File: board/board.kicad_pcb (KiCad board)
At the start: 2 copper layers, 26.5 x 7.5 mm, 10 parts, among them Q1 2N7002, U1 ATtiny402-SS

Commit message: fixed schematic and pcb
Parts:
- added C3: 10u, Capacitor_SMD:C_0603_1608Metric_Pad1.08x0.95mm_HandSolder, F.Cu at (99.1, 76.0)
- added G***: LOGO, LOGO, B.Cu at (84.3, 77.8)
- added TP1: TestPoint, TestPoint:TestPoint_Pad_D1.0mm, B.Cu at (96.3, 80.3)
- Q1: value 2N7002 -> AO3401A
- moved Q1 0.63 mm to (99.1, 78.8), turned to -90 degrees
- moved U3 0.55 mm to (103.4, 82.3)
- moved R1 0.44 mm to (94.6, 77.6)
- moved R2 0.44 mm to (94.6, 76.2), turned to 180 degrees
- moved R3 0.44 mm to (94.6, 79.1)
- moved R4 0.44 mm to (94.6, 80.5)
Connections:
- C2 pad 2: GND_BT -> GND
- Q1 pad 2: GND -> +4V
- Q1 pad 3: GND_BT -> Vcc_BT
- R2 pad 1: GND -> Net-(Q1-G)
- R2 pad 2: Net-(Q1-G) -> +4V
- U1 pad 2: unconnected-(U1-PA6-Pad2) -> IO_SCAN
- U3 pad 1: +4V -> Vcc_BT
- U3 pad 3: UPDI -> IO_SCAN
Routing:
- net IO_SCAN: track 0.00 -> 17.8 mm, vias 0 -> 2
- net GND_BT: track 10.4 -> 0.00 mm
- net Vcc_BT: track 0.00 -> 10.3 mm
- net GND: track 11.9 -> 3.34 mm, vias 5 -> 3
- net UPDI: track 9.41 -> 3.62 mm, vias 0 -> 1
- net INT_SW: track 20.5 -> 15.0 mm
- net +4V: track 27.1 -> 22.9 mm, vias 2 -> 4
- net Net-(Q1-G): track 6.41 -> 8.00 mm
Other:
- board size 26.5 x 7.5 mm -> 26 x 7.5 mm

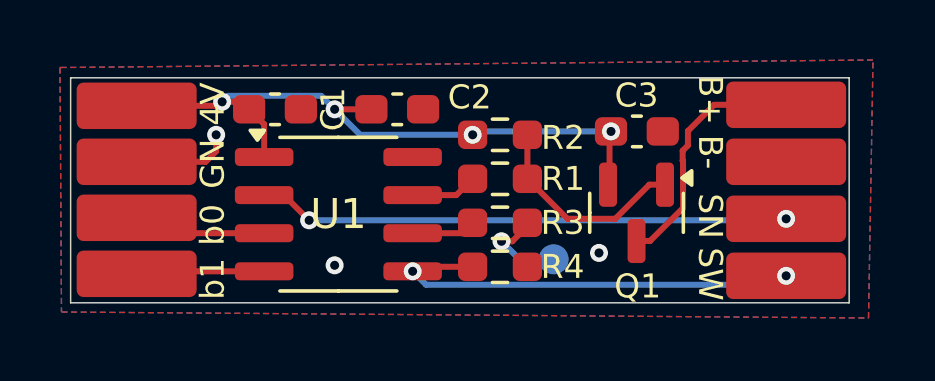
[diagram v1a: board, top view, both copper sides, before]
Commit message: pcb tweaks and gitignore
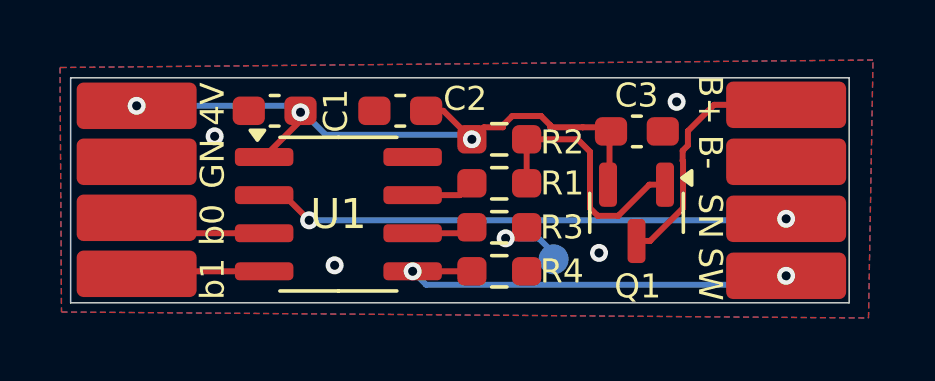
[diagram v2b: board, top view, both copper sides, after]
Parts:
- moved R3 0.15 mm to (94.5, 79.2)
- moved R4 0.15 mm to (94.5, 80.7)
- moved R1 0.15 mm to (94.5, 77.8)
- moved R2 0.15 mm to (94.5, 76.3)
- moved C2 0.11 mm to (91.2, 75.3), turned to 180 degrees
- moved C1 0.05 mm to (87.0, 75.3), turned to 180 degrees
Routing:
- net GND: track 3.34 -> 0.35 mm, vias 3 -> 4
- net Net-(Q1-G): track 8.00 -> 9.59 mm
- net UPDI: track 3.62 -> 3.12 mm
- net +4V: track 22.9 -> 23.2 mm, vias 4 -> 3

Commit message: added 4v via
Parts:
- moved R2 0.07 mm to (94.5, 76.4)
- moved R1 0.07 mm to (94.5, 77.8)
- moved R3 0.07 mm to (94.5, 79.3)
- moved R4 0.07 mm to (94.5, 80.8)
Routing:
- net +4V: track 23.2 -> 22.7 mm, vias 3 -> 4
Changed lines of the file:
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@@
 	(footprint "Resistor_SMD:R_0603_1608Metric_Pad0.98x0.95mm_HandSolder"
 		(layer "F.Cu")
-		(at 94.5375 77.766667 180)
+		(at 94.55 77.833334 180)
 		(descr "Resistor SMD 0603 (1608 Metric), square (rectangular) end terminal, IPC-7351 nominal with elongated pad for handsoldering. (Body size source: IPC-SM-782 page 72, https://www.pcb-3d.com/wordpress/wp-content/uploads/ipc-sm-782a_amendment_1_and_2.pdf), generated with kicad-footprint-generator")
 		(tags "resistor handsolder")
@@
 	(footprint "Resistor_SMD:R_0603_1608Metric_Pad0.98x0.95mm_HandSolder"
 		(layer "F.Cu")
-		(at 94.5375 80.7 180)
+		(at 94.55 80.766667 180)
 		(descr "Resistor SMD 0603 (1608 Metric), square (rectangular) end terminal, IPC-7351 nominal with elongated pad for handsoldering. (Body size source: IPC-SM-782 page 72, https://www.pcb-3d.com/wordpress/wp-content/uploads/ipc-sm-782a_amendment_1_and_2.pdf), generated with kicad-footprint-generator")
 		(tags "resistor handsolder")
@@
 	(footprint "Resistor_SMD:R_0603_1608Metric_Pad0.98x0.95mm_HandSolder"
 		(layer "F.Cu")
-		(at 94.5375 79.233333 180)
+		(at 94.55 79.3 180)
 		(descr "Resistor SMD 0603 (1608 Metric), square (rectangular) end terminal, IPC-7351 nominal with elongated pad for handsoldering. (Body size source: IPC-SM-782 page 72, https://www.pcb-3d.com/wordpress/wp-content/uploads/ipc-sm-782a_amendment_1_and_2.pdf), generated with kicad-footprint-generator")
 		(tags "resistor handsolder")
@@
 	(footprint "Resistor_SMD:R_0603_1608Metric_Pad0.98x0.95mm_HandSolder"
 		(layer "F.Cu")
-		(at 94.5375 76.3 180)
+		(at 94.55 76.366667 180)
 		(descr "Resistor SMD 0603 (1608 Metric), square (rectangular) end terminal, IPC-7351 nominal with elongated pad for handsoldering. (Body size source: IPC-SM-782 page 72, https://www.pcb-3d.com/wordpress/wp-content/uploads/ipc-sm-782a_amendment_1_and_2.pdf), generated with kicad-footprint-generator")
 		(tags "resistor handsolder")
@@
 	)
 	(via
-		(at 100.45 75.05)
+		(at 94.65 75.05)
 		(size 0.6)
 		(drill 0.3)
@@
 	)
 	(segment
-		(start 96.2385 75.832866)
-		(end 96.2385 75.899)
-		(width 0.2)
-		(layer "F.Cu")
-		(net 2)
-	)
-	(segment
 		(start 87.9125 75.6775)
 		(end 87.9125 75.4)
@@
 	)
 	(segment
-		(start 98.125 75.9)
-		(end 98.2625 76.0375)
-		(width 0.2)
-		(layer "F.Cu")
-		(net 2)
-	)
-	(segment
 		(start 86.7 76.89)
 		(end 87.9125 75.6775)
@@
 	)
 	(segment
-		(start 96.2385 75.899)
-		(end 97.3161 75.899)
-		(width 0.2)
-		(layer "F.Cu")
-		(net 2)
-	)
-	(segment
 		(start 92.675 75.35)
 		(end 93.625 76.3)
@@
 	)
 	(segment
-		(start 95.929634 75.524)
-		(end 96.2385 75.832866)
-		(width 0.2)
-		(layer "F.Cu")
-		(net 2)
-	)
-	(segment
-		(start 94.970366 75.524)
-		(end 95.929634 75.524)
-		(width 0.2)
-		(layer "F.Cu")
-		(net 2)
-	)
-	(segment
-		(start 93.625 76.3)
-		(end 93.625 75.9625)
-		(width 0.2)
-		(layer "F.Cu")
-		(net 2)
-	)
-	(segment
-		(start 97.3171 75.9)
-		(end 98.125 75.9)
+		(start 93.6375 76.366667)
+		(end 93.6375 76.029167)
 		(width 0.2)
 		(layer "F.Cu")
@@
 	)
 	(segment
-		(start 93.625 76.3)
-		(end 94.025 75.9)
-		(width 0.2)
-		(layer "F.Cu")
-		(net 2)
-	)
-	(segment
-		(start 94.6615 75.832866)
-		(end 94.970366 75.524)
-		(width 0.2)
-		(layer "F.Cu")
-		(net 2)
-	)
-	(segment
-		(start 94.6615 75.9)
-		(end 94.6615 75.832866)
-		(width 0.2)
-		(layer "F.Cu")
-		(net 2)
-	)
-	(segment
 		(start 98.2125 76.0875)
 		(end 98.2625 76.0375)
-		(width 0.2)
-		(layer "F.Cu")
-		(net 2)
-	)
-	(segment
-		(start 94.025 75.9)
-		(end 94.6615 75.9)
-		(width 0.2)
-		(layer "F.Cu")
-		(net 2)
-	)
-	(segment
-		(start 97.3161 75.899)
-		(end 97.3171 75.9)
 		(width 0.2)
 		(layer "F.Cu")
@@
 	)
 	(via
-		(at 93.625 76.3)
+		(at 98.2625 76.0375)
+		(size 0.6)
+		(drill 0.3)
+		(layers "F.Cu" "B.Cu")
+		(net 2)
+	)
+	(via
+		(at 93.6375 76.366667)
 		(size 0.6)
 		(drill 0.3)
@@
 	)
 	(segment
+		(start 93.966667 76.0375)
+		(end 93.6375 76.366667)
+		(width 0.2)
+		(layer "B.Cu")
+		(net 2)
+	)
+	(segment
 		(start 82.45 75.183333)
 		(end 87.695833 75.183333)
@@
 	)
 	(segment
+		(start 98.2625 76.0375)
+		(end 93.966667 76.0375)
+		(width 0.2)
+		(layer "B.Cu")
+		(net 2)
+	)
+	(segment
 		(start 93.775 76.15)
 		(end 93.625 76.3)
@@
 	)
 	(segment
-		(start 95.7625 76.3)
-		(end 95.45 76.3)
+		(start 95.775 76.366667)
+		(end 95.4625 76.366667)
 		(width 0.2)
 		(layer "F.Cu")
@@
 	)
 	(segment
-		(start 95.504167 77.766667)
-		(end 95.45 77.766667)
+		(start 95.516667 77.833334)
+		(end 95.4625 77.833334)
 		(width 0.2)
 		(layer "F.Cu")
@@
 	)
 	(segment
-		(start 95.6 76.45)
-		(end 95.45 76.3)
+		(start 95.6125 76.516667)
+		(end 95.4625 76.366667)
 		(width 0.2)
 		(layer "F.Cu")
@@
 	)
 	(segment
-		(start 95.45 77.766667)
-		(end 95.45 78.1125)
+		(start 95.4625 77.833334)
+		(end 95.4625 78.179167)
 		(width 0.2)
 		(layer "F.Cu")
@@
 	)
 	(segment
-		(start 95.45 77.766667)
-		(end 95.45 76.3)
+		(start 95.4625 77.833334)
+		(end 95.4625 76.366667)
 		(width 0.2)
 		(layer "F.Cu")
@@
 	)
 	(segment
+		(start 93.310834 78.16)
+		(end 93.6375 77.833334)
+		(width 0.2)
+		(layer "F.Cu")
+		(net 4)
+	)
+	(segment
 		(start 91.65 78.16)
-		(end 93.231667 78.16)
+		(end 93.310834 78.16)
 		(width 0.2)
 		(layer "F.Cu")
@@
 	)
 	(segment
-		(start 93.231667 78.16)
-		(end 93.625 77.766667)
-		(width 0.2)
-		(layer "F.Cu")
-		(net 4)
-	)
-	(segment
-		(start 95.19742 79.6)
-		(end 95.45 79.34742)
+		(start 95.4625 79.414087)
+		(end 95.4625 79.3)
 		(width 0.2)
 		(layer "F.Cu")
@@
 	)
 	(segment
-		(start 94.75 79.6)
-		(end 95.19742 79.6)
+		(start 94.633467 79.666667)
+		(end 95.20992 79.666667)
 		(width 0.2)
 		(layer "F.Cu")
@@
 	)
 	(segment
-		(start 95.584333 79.099)
-		(end 95.45 79.233333)
+		(start 95.20992 79.666667)
+		(end 95.4625 79.414087)
 		(width 0.2)
 		(layer "F.Cu")
@@
 	)
 	(segment
-		(start 95.45 79.34742)
-		(end 95.45 79.233333)
+		(start 94.608862 79.691272)
+		(end 94.633467 79.666667)
 		(width 0.2)
 		(layer "F.Cu")
 		(net 5)
 	)
+	(segment
+		(start 95.596833 79.165667)
+		(end 95.4625 79.3)
+		(width 0.2)
+		(layer "F.Cu")
+		(net 5)
+	)
 	(via
-		(at 94.75 79.6)
+		(at 94.608862 79.691272)
 		(size 0.6)
 		(drill 0.3)
@@
 	)
 	(segment
+		(start 93.5075 79.43)
+		(end 93.6375 79.3)
+		(width 0.2)
+		(layer "F.Cu")
+		(net 6)
+	)
+	(segment
+		(start 93.440833 79.496667)
+		(end 93.6375 79.3)
+		(width 0.2)
+		(layer "F.Cu")
+		(net 6)
+	)
+	(segment
+		(start 93.290833 79.646667)
+		(end 93.6375 79.3)
+		(width 0.2)
+		(layer "F.Cu")
+		(net 6)
+	)
+	(segment
 		(start 91.65 79.43)
-		(end 93.428333 79.43)
-		(width 0.2)
-		(layer "F.Cu")
-		(net 6)
-	)
-	(segment
-		(start 93.428333 79.43)
-		(end 93.625 79.233333)
-		(width 0.2)
-		(layer "F.Cu")
-		(net 6)
-	)
-	(segment
-		(start 93.278333 79.58)
-		(end 93.625 79.233333)
+		(end 93.5075 79.43)
 		(width 0.2)
 		(layer "F.Cu")
@@
 	)
 	(segment
-		(start 91.65 80.7)
-		(end 93.625 80.7)
+		(start 91.716667 80.766667)
+		(end 91.65 80.7)
 		(width 0.2)
 		(layer "F.Cu")
@@
 	)
 	(segment
-		(start 93.525 80.8)
-		(end 93.625 80.7)
+		(start 93.5375 80.866667)
+		(end 93.6375 80.766667)
 		(width 0.2)
 		(layer "F.Cu")
@@
 		(width 0.2)
 		(layer "F.Cu")
+		(net 7)
+	)
+	(segment
+		(start 93.6375 80.766667)
+		(end 91.716667 80.766667)
+		(width 0.2)
+		(layer "F.Cu")
